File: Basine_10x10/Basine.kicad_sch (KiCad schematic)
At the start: 55 parts, among them J1 2060-451/998-404, J10 2060-451/998-404, J11 2060-451/998-404, J12 2060-451/998-404, J13 2060-451/998-404, J14 2060-451/998-404, J15 2060-451/998-404, J16 2060-451/998-404, J2 2060-451/998-404, J3 2060-451/998-404, J4 2060-451/998-404, J5 2060-451/998-404, J6 2060-451/998-404, J7 2060-451/998-404, J8 2060-451/998-404, J9 2060-451/998-404

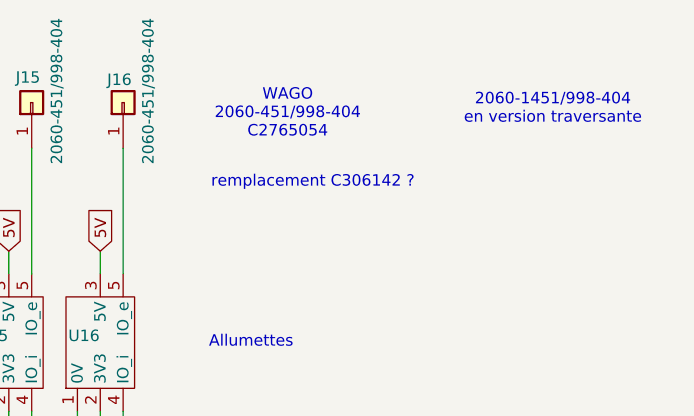
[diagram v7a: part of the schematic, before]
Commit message: 10x10
chgt connecteur wago
fabrication
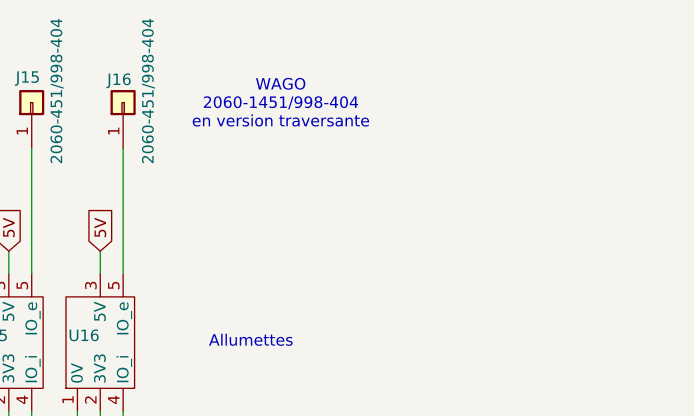
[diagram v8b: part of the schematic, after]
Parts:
- J1, J10, J11, J12, J13, J14, J15, J16, J2, J3, J4, J5, J6, J7, J8, J9: footprint Chimere_comps:CONN_2060-451_998-404_WAGO -> Chimere_comps:CONN_2060-1451_998-404_WAGO; LCSC C2765054 -> (none); now left out of the parts list
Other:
- note added: "WAGO 2060-1451/998-404 en version traversante"
- note removed: "2060-1451/998-404 en version traversante"
- note removed: "WAGO 2060-451/998-404 C2765054"
- note removed: "remplacement C306142 ?"
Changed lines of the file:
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@@
 		)
 	)
-	(text "2060-1451/998-404\nen version traversante"
+	(text "WAGO\n2060-1451/998-404\nen version traversante"
 		(exclude_from_sim no)
-		(at 228.092 22.352 0)
+		(at 197.866 21.844 0)
 		(effects
 			(font
@@
 		)
 	)
-	(text "remplacement C306142 ?"
-		(exclude_from_sim no)
-		(at 201.422 30.48 0)
-		(effects
-			(font
-				(size 1.27 1.27)
-			)
-		)
-	)
-	(text "WAGO\n2060-451/998-404\nC2765054"
-		(exclude_from_sim no)
-		(at 198.628 22.86 0)
-		(effects
-			(font
-				(size 1.27 1.27)
-			)
-		)
-	)
 	(global_label "24V"
 		(shape input)
@@
 		(unit 1)
 		(exclude_from_sim no)
-		(in_bom yes)
+		(in_bom no)
 		(on_board yes)
 		(dnp no)
@@
 			)
 		)
-		(property "Footprint" "Chimere_comps:CONN_2060-451_998-404_WAGO"
+		(property "Footprint" "Chimere_comps:CONN_2060-1451_998-404_WAGO"
 			(at 160.02 21.59 0)
 			(effects
@@
 			)
 		)
-		(property "LCSC" "C2765054"
-			(at 160.02 21.59 0)
-			(effects
-				(font
-					(size 1.27 1.27)
-				)
-				(hide yes)
-			)
-		)
 		(pin "1"
 		)
@@
 		(unit 1)
 		(exclude_from_sim no)
-		(in_bom yes)
+		(in_bom no)
 		(on_board yes)
 		(dnp no)
@@
 			)
 		)
-		(property "Footprint" "Chimere_comps:CONN_2060-451_998-404_WAGO"
+		(property "Footprint" "Chimere_comps:CONN_2060-1451_998-404_WAGO"
 			(at 44.45 21.59 0)
 			(effects
@@
 			)
 		)
-		(property "LCSC" "C2765054"
-			(at 44.45 21.59 0)
-			(effects
-				(font
-					(size 1.27 1.27)
-				)
-				(hide yes)
-			)
-		)
 		(pin "1"
 		)
@@
 		(unit 1)
 		(exclude_from_sim no)
-		(in_bom yes)
+		(in_bom no)
 		(on_board yes)
 		(dnp no)
@@
 			)
 		)
-		(property "Footprint" "Chimere_comps:CONN_2060-451_998-404_WAGO"
+		(property "Footprint" "Chimere_comps:CONN_2060-1451_998-404_WAGO"
 			(at 20.32 21.59 0)
 			(effects
@@
 			)
 		)
-		(property "LCSC" "C2765054"
-			(at 20.32 21.59 0)
-			(effects
-				(font
-					(size 1.27 1.27)
-				)
-				(hide yes)
-			)
-		)
 		(pin "1"
 		)
@@
 		(unit 1)
 		(exclude_from_sim no)
-		(in_bom yes)
+		(in_bom no)
 		(on_board yes)
 		(dnp no)
@@
 			)
 		)
-		(property "Footprint" "Chimere_comps:CONN_2060-451_998-404_WAGO"
+		(property "Footprint" "Chimere_comps:CONN_2060-1451_998-404_WAGO"
 			(at 129.54 21.59 0)
 			(effects
@@
 			)
 		)
-		(property "LCSC" "C2765054"
-			(at 129.54 21.59 0)
-			(effects
-				(font
-					(size 1.27 1.27)
-				)
-				(hide yes)
-			)
-		)
 		(pin "1"
 		)
@@
 		(unit 1)
 		(exclude_from_sim no)
-		(in_bom yes)
+		(in_bom no)
 		(on_board yes)
 		(dnp no)
@@
 			)
 		)
-		(property "Footprint" "Chimere_comps:CONN_2060-451_998-404_WAGO"
+		(property "Footprint" "Chimere_comps:CONN_2060-1451_998-404_WAGO"
 			(at 50.8 21.59 0)
 			(effects
@@
 			)
 		)
-		(property "LCSC" "C2765054"
-			(at 50.8 21.59 0)
-			(effects
-				(font
-					(size 1.27 1.27)
-				)
-				(hide yes)
-			)
-		)
 		(pin "1"
 		)
@@
 		(unit 1)
 		(exclude_from_sim no)
-		(in_bom yes)
+		(in_bom no)
 		(on_board yes)
 		(dnp no)
@@
 			)
 		)
-		(property "Footprint" "Chimere_comps:CONN_2060-451_998-404_WAGO"
+		(property "Footprint" "Chimere_comps:CONN_2060-1451_998-404_WAGO"
 			(at 119.38 21.59 0)
 			(effects
@@
 			)
 		)
-		(property "LCSC" "C2765054"
-			(at 119.38 21.59 0)
-			(effects
-				(font
-					(size 1.27 1.27)
-				)
-				(hide yes)
-			)
-		)
 		(pin "1"
 		)
@@
 		(unit 1)
 		(exclude_from_sim no)
-		(in_bom yes)
+		(in_bom no)
 		(on_board yes)
 		(dnp no)
@@
 			)
 		)
-		(property "Footprint" "Chimere_comps:CONN_2060-451_998-404_WAGO"
+		(property "Footprint" "Chimere_comps:CONN_2060-1451_998-404_WAGO"
 			(at 180.34 21.59 0)
 			(effects
@@
 			)
 		)
-		(property "LCSC" "C2765054"
-			(at 180.34 21.59 0)
-			(effects
-				(font
-					(size 1.27 1.27)
-				)
-				(hide yes)
-			)
-		)
 		(pin "1"
 		)
@@
 		(unit 1)
 		(exclude_from_sim no)
-		(in_bom yes)
+		(in_bom no)
 		(on_board yes)
 		(dnp no)
@@
 			)
 		)
-		(property "Footprint" "Chimere_comps:CONN_2060-451_998-404_WAGO"
+		(property "Footprint" "Chimere_comps:CONN_2060-1451_998-404_WAGO"
 			(at 88.9 21.59 0)
 			(effects
@@
 			)
 		)
-		(property "LCSC" "C2765054"
-			(at 88.9 21.59 0)
-			(effects
-				(font
-					(size 1.27 1.27)
-				)
-				(hide yes)
-			)
-		)
 		(pin "1"
 		)
@@
 		(unit 1)
 		(exclude_from_sim no)
-		(in_bom yes)
+		(in_bom no)
 		(on_board yes)
 		(dnp no)
@@
 			)
 		)
-		(property "Footprint" "Chimere_comps:CONN_2060-451_998-404_WAGO"
+		(property "Footprint" "Chimere_comps:CONN_2060-1451_998-404_WAGO"
 			(at 149.86 21.59 0)
 			(effects
@@
 			)
 		)
-		(property "LCSC" "C2765054"
-			(at 149.86 21.59 0)
-			(effects
-				(font
-					(size 1.27 1.27)
-				)
-				(hide yes)
-			)
-		)
 		(pin "1"
 		)
@@
 		(unit 1)
 		(exclude_from_sim no)
-		(in_bom yes)
+		(in_bom no)
 		(on_board yes)
 		(dnp no)
@@
 			)
 		)
-		(property "Footprint" "Chimere_comps:CONN_2060-451_998-404_WAGO"
+		(property "Footprint" "Chimere_comps:CONN_2060-1451_998-404_WAGO"
 			(at 109.22 21.59 0)
 			(effects
@@
 			)
 		)
-		(property "LCSC" "C2765054"
-			(at 109.22 21.59 0)
-			(effects
-				(font
-					(size 1.27 1.27)
-				)
-				(hide yes)
-			)
-		)
 		(pin "1"
 		)
@@
 		(unit 1)
 		(exclude_from_sim no)
-		(in_bom yes)
+		(in_bom no)
 		(on_board yes)
 		(dnp no)
@@
 			)
 		)
-		(property "Footprint" "Chimere_comps:CONN_2060-451_998-404_WAGO"
+		(property "Footprint" "Chimere_comps:CONN_2060-1451_998-404_WAGO"
 			(at 139.7 21.59 0)
 			(effects
@@
 			)
 		)
-		(property "LCSC" "C2765054"
-			(at 139.7 21.59 0)
-			(effects
-				(font
-					(size 1.27 1.27)
-				)
-				(hide yes)
-			)
-		)
 		(pin "1"
 		)
@@
 		(unit 1)
 		(exclude_from_sim no)
-		(in_bom yes)
+		(in_bom no)
 		(on_board yes)
 		(dnp no)
@@
 			)
 		)
-		(property "Footprint" "Chimere_comps:CONN_2060-451_998-404_WAGO"
+		(property "Footprint" "Chimere_comps:CONN_2060-1451_998-404_WAGO"
 			(at 99.06 21.59 0)
 			(effects
@@
 			)
 		)
-		(property "LCSC" "C2765054"
-			(at 99.06 21.59 0)
-			(effects
-				(font
-					(size 1.27 1.27)
-				)
-				(hide yes)
-			)
-		)
 		(pin "1"
 		)
@@
 		(unit 1)
 		(exclude_from_sim no)
-		(in_bom yes)
+		(in_bom no)
 		(on_board yes)
 		(dnp no)
@@
 			)
 		)
-		(property "Footprint" "Chimere_comps:CONN_2060-451_998-404_WAGO"
+		(property "Footprint" "Chimere_comps:CONN_2060-1451_998-404_WAGO"
 			(at 68.58 21.59 0)
 			(effects
@@
 			)
 		)
-		(property "LCSC" "C2765054"
-			(at 68.58 21.59 0)
-			(effects
-				(font
-					(size 1.27 1.27)
-				)
-				(hide yes)
-			)
-		)
 		(pin "1"
 		)
@@
 		(unit 1)
 		(exclude_from_sim no)
-		(in_bom yes)
+		(in_bom no)
 		(on_board yes)
 		(dnp no)
@@
 			)
 		)
-		(property "Footprint" "Chimere_comps:CONN_2060-451_998-404_WAGO"
+		(property "Footprint" "Chimere_comps:CONN_2060-1451_998-404_WAGO"
 			(at 78.74 21.59 0)
 			(effects
@@
 			)
 		)
-		(property "LCSC" "C2765054"
-			(at 78.74 21.59 0)
-			(effects
-				(font
-					(size 1.27 1.27)
-				)
-				(hide yes)
-			)
-		)
 		(pin "1"
 		)
@@
 		(unit 1)
 		(exclude_from_sim no)
-		(in_bom yes)
+		(in_bom no)
 		(on_board yes)
 		(dnp no)
@@
 			)
 		)
-		(property "Footprint" "Chimere_comps:CONN_2060-451_998-404_WAGO"
+		(property "Footprint" "Chimere_comps:CONN_2060-1451_998-404_WAGO"
 			(at 26.67 21.59 0)
 			(effects
@@
 			)
 		)
-		(property "LCSC" "C2765054"
-			(at 26.67 21.59 0)
-			(effects
-				(font
-					(size 1.27 1.27)
-				)
-				(hide yes)
-			)
-		)
 		(pin "1"
 		)
@@
 		(unit 1)
 		(exclude_from_sim no)
-		(in_bom yes)
+		(in_bom no)
 		(on_board yes)
 		(dnp no)
@@
 			)
 		)
-		(property "Footprint" "Chimere_comps:CONN_2060-451_998-404_WAGO"
+		(property "Footprint" "Chimere_comps:CONN_2060-1451_998-404_WAGO"
 			(at 170.18 21.59 0)
 			(effects
@@
 			(at 170.18 21.59 0)
 			(effects
-				(font
-					(size 1.27 1.27)
-				)
-				(hide yes)
-			)
-		)
-		(property "LCSC" "C2765054"
-			(at 170.18 21.59 0)
-			(effects
